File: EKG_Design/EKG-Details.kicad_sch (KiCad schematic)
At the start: 10 parts

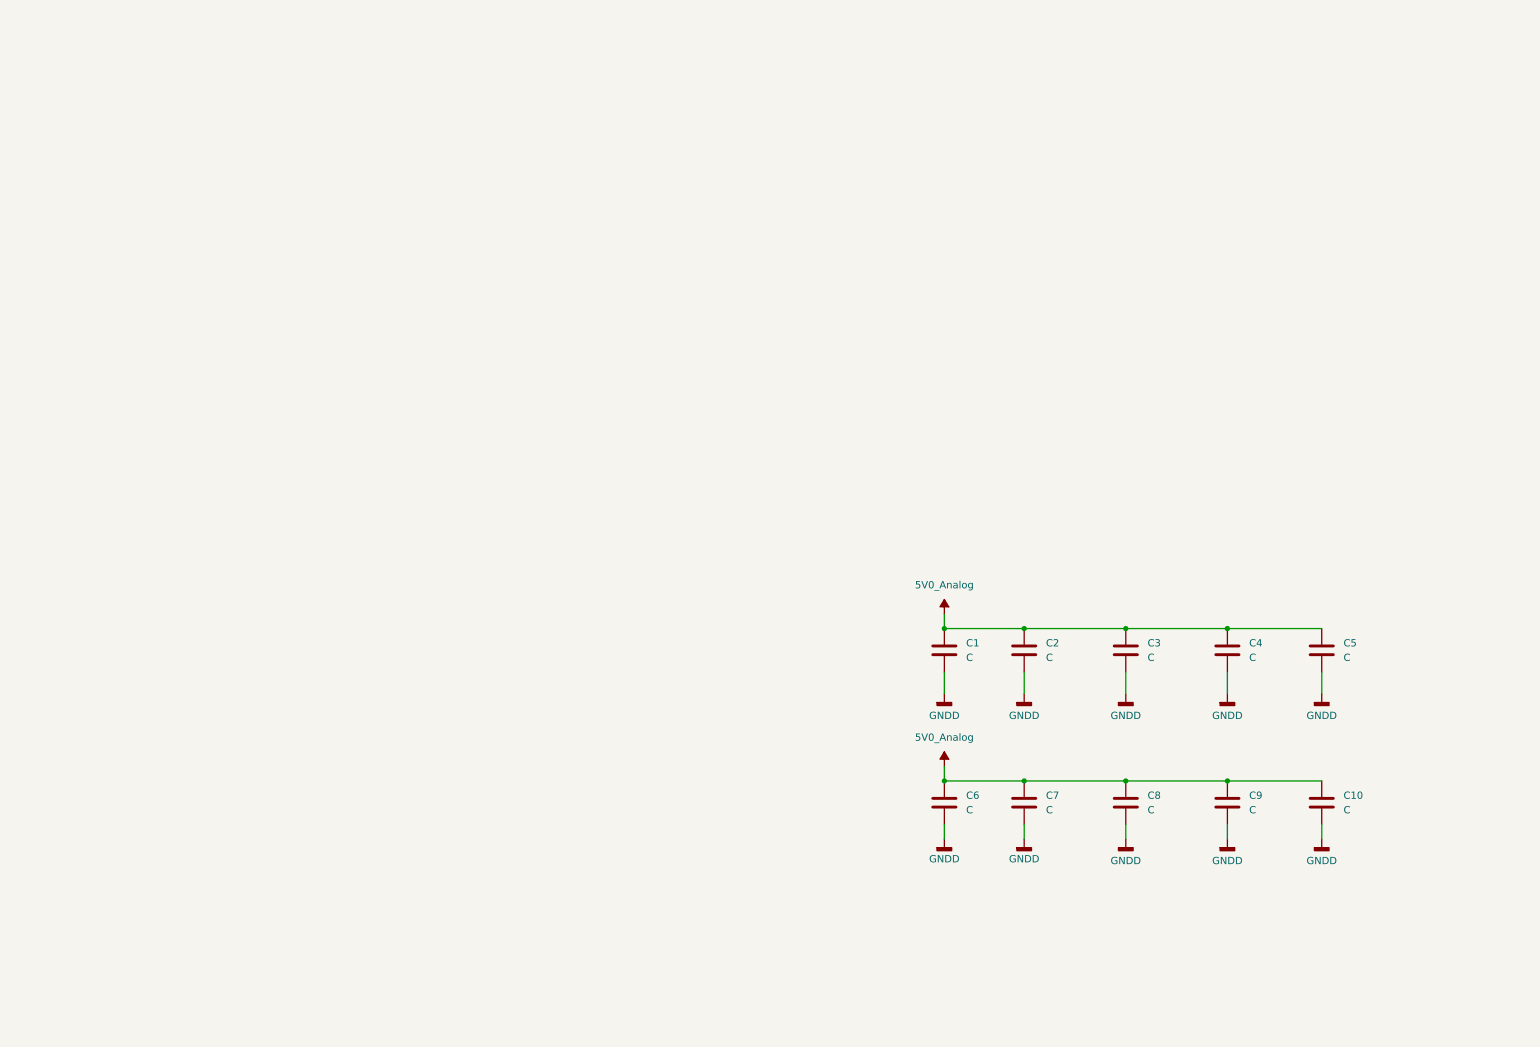
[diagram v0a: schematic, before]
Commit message: Started EKG-Details and ECG-PulseDetection Circuit Symbols implemented
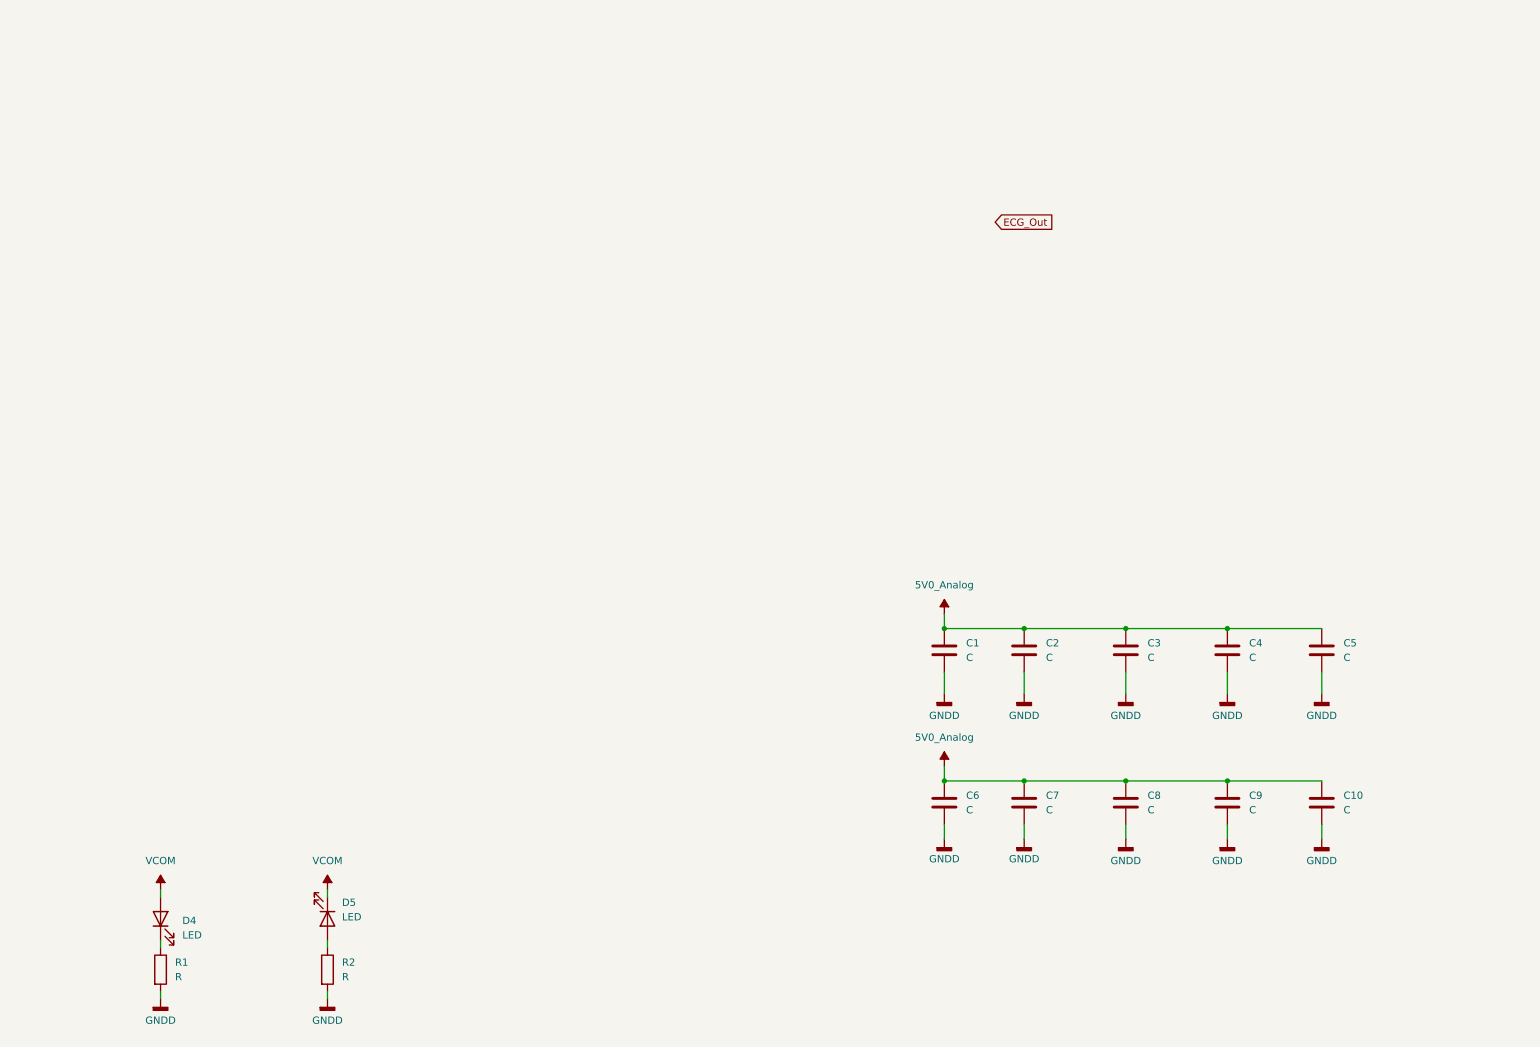
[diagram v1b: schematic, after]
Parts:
- added D4, D5: LED, symbol Device:LED
- added R1, R2: R, symbol Device:R
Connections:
- net GNDD: now also R1.2, R2.2
- new net: D4.1 (K), R1.1
- new net: D5.2 (A), R2.1
- new net VCOM: D4.2 (A), D5.1 (K)
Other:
- company: (none) -> HAWK
- title: (none) -> EKG-Verstärker

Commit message: EKG-Details updated
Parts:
- added J1, J2: Conn_01x02_Pin, symbol Connector:Conn_01x02_Pin
- added R5, R6, R7, R8: R, symbol Device:R
- added U1: OPA2156xDGK, Package_SO:VSSOP-8_3x3mm_P0.65mm, symbol Amplifier_Operational:OPA2156xDGK
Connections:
- new net: R6.2, U1.5 (+)
- new net: J2.1 (Pin_1), U1.6 (-), U1.7
- new net: J1.1 (Pin_1), R5.1
- new net: R5.2, U1.2 (-)
- new net: J1.2 (Pin_2), U1.1, U1.3 (+)
- new net: J2.2 (Pin_2), R6.1

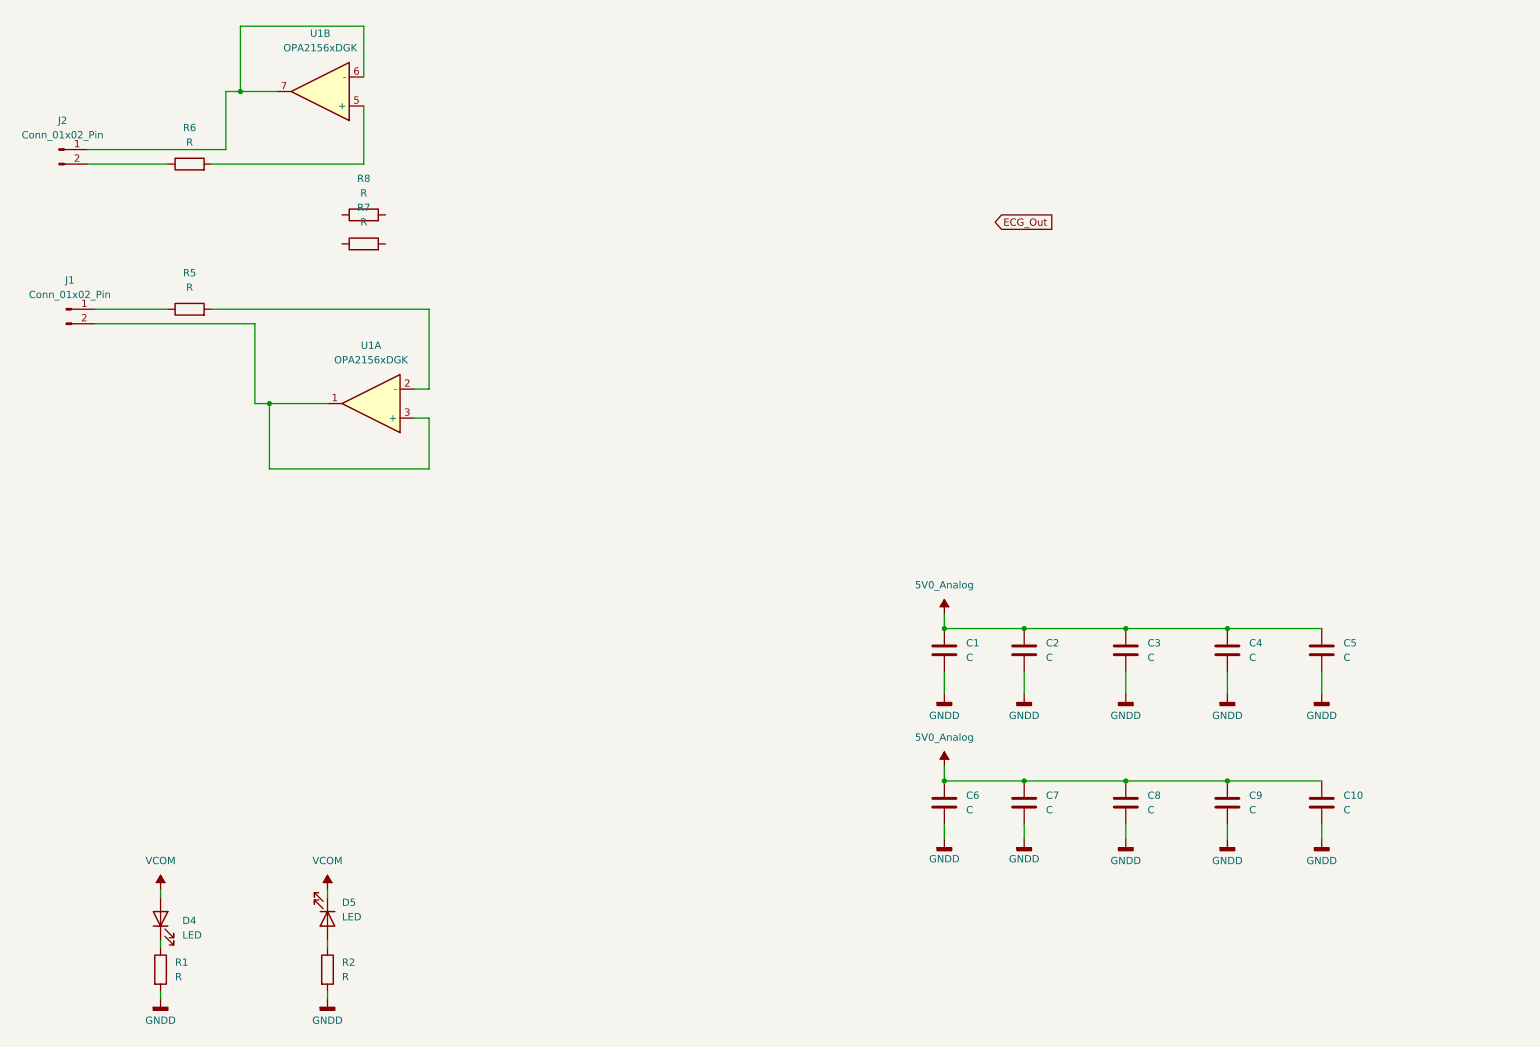
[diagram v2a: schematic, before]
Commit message: EKG-Details basic schematic, still needs cleaning
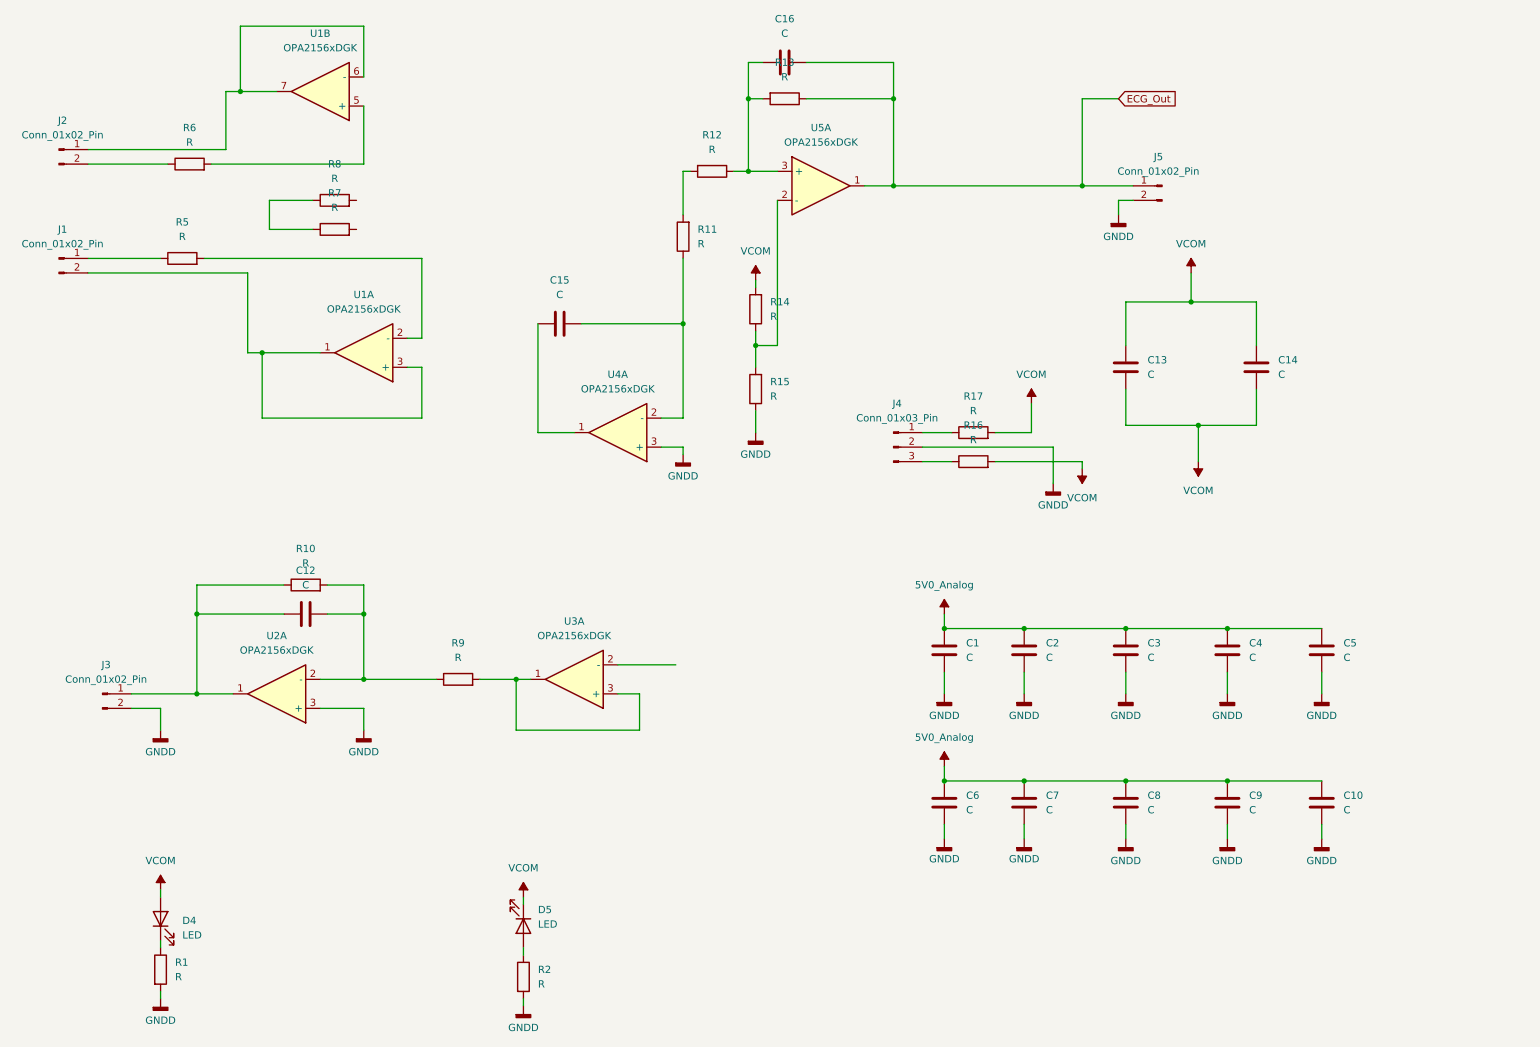
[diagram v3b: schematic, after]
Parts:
- added C12, C13, C14, C15, C16: C, symbol Device:C
- added J3, J5: Conn_01x02_Pin, symbol Connector:Conn_01x02_Pin
- added J4: Conn_01x03_Pin, symbol Connector:Conn_01x03_Pin
- added R10, R11, R12, R13, R14, R15, R16, R17, R9: R, symbol Device:R
- added U2, U3, U4, U5: OPA2156xDGK, Package_SO:VSSOP-8_3x3mm_P0.65mm, symbol Amplifier_Operational:OPA2156xDGK
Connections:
- net ECG_Out: now also C16.2, J5.1 (Pin_1), R13.1, U5.1
- net GNDD: now also J3.2 (Pin_2), J4.2 (Pin_2), J5.2 (Pin_2), R15.1, U2.3 (+), U4.3 (+)
- net VCOM: now also C13.1, C13.2, C14.1, C14.2, R14.2, R16.2, R17.2
- net at R8.1: now also R7.1
- new net: C16.1, R12.1, R13.2, U5.3 (+)
- new net: R11.2, R12.2
- new net: C12.1, J3.1 (Pin_1), R10.1, U2.1
- new net: C12.2, R10.2, R9.1, U2.2 (-)
- new net: C15.1, U4.1
- new net: C15.2, R11.1, U4.2 (-)
- new net: R14.1, R15.2, U5.2 (-)
- new net: J4.1 (Pin_1), R17.1
- new net: R9.2, U3.1, U3.3 (+)
- new net: J4.3 (Pin_3), R16.1
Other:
- moved on the sheet: D5, J1, R2, R5, R7, R8, U1A

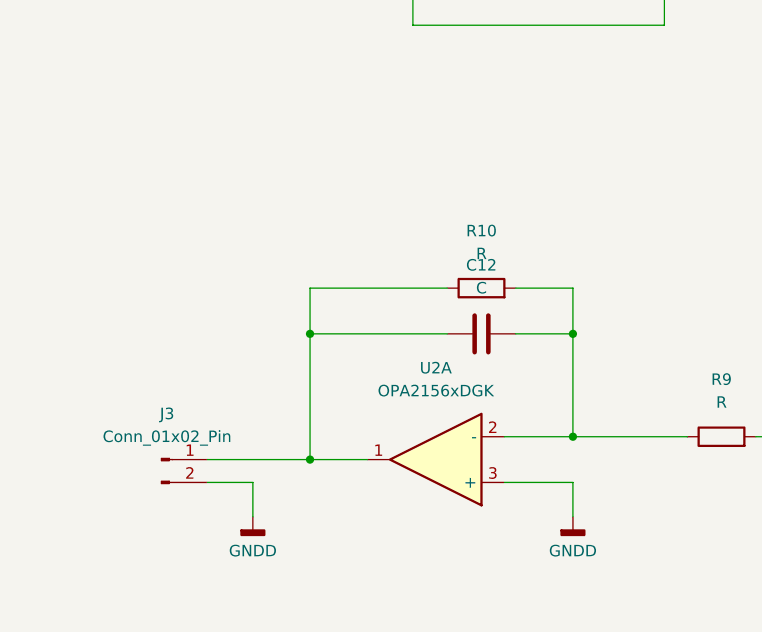
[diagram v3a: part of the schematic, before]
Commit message: EKG-Details basic schematic, still needs a little cleaning
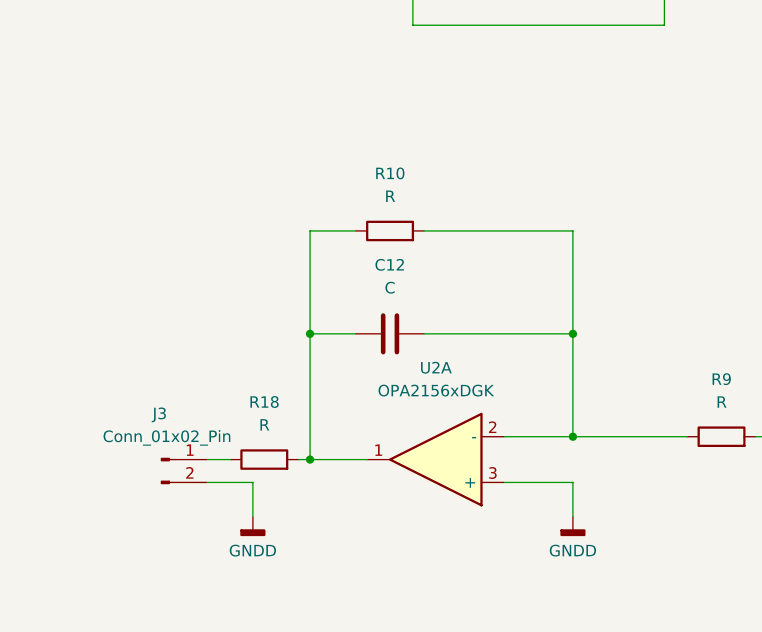
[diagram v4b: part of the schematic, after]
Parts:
- added R18: R, symbol Device:R
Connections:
- net at C12.1, R10.1, U2.1: now also R18.2; no longer J3.1 (Pin_1)
- new net: J3.1 (Pin_1), R18.1
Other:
- moved on the sheet: C12, R10
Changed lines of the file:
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@@
 	)
 	(junction
-		(at 137.16 67.31)
+		(at 52.07 118.11)
 		(diameter 0)
 		(color 0 0 0 0)
 	)
 	(junction
-		(at 227.33 85.09)
+		(at 137.16 67.31)
 		(diameter 0)
 		(color 0 0 0 0)
 	)
 	(junction
-		(at 52.07 118.11)
+		(at 227.33 85.09)
 		(diameter 0)
 		(color 0 0 0 0)
@@
 	)
 	(junction
-		(at 52.07 132.08)
+		(at 81.28 118.11)
 		(diameter 0)
 		(color 0 0 0 0)
@@
 	)
 	(junction
-		(at 81.28 118.11)
-		(diameter 0)
-		(color 0 0 0 0)
-	)
-	(junction
 		(at 107.95 129.54)
 		(diameter 0)
@@
 	)
 	(junction
+		(at 52.07 132.08)
+		(diameter 0)
+		(color 0 0 0 0)
+	)
+	(junction
 		(at 232.41 147.32)
 		(diameter 0)
@@
 	(wire
 		(pts
-			(xy 67.31 118.11) (xy 52.07 118.11)
+			(xy 57.15 118.11) (xy 52.07 118.11)
 		)
 		(stroke
@@
 	(wire
 		(pts
-			(xy 81.28 118.11) (xy 74.93 118.11)
+			(xy 81.28 118.11) (xy 64.77 118.11)
 		)
 		(stroke
@@
 	(wire
 		(pts
-			(xy 52.07 118.11) (xy 52.07 132.08)
-		)
-		(stroke
-			(width 0)
-			(type default)
-		)
-	)
-	(wire
-		(pts
 			(xy 213.36 45.72) (xy 215.9 45.72)
 		)
@@
 	(wire
 		(pts
-			(xy 81.28 113.03) (xy 81.28 118.11)
+			(xy 81.28 106.68) (xy 81.28 118.11)
 		)
 		(stroke
@@
 	(wire
 		(pts
-			(xy 40.64 132.08) (xy 52.07 132.08)
-		)
-		(stroke
-			(width 0)
-			(type default)
-		)
-	)
-	(wire
-		(pts
 			(xy 81.28 134.62) (xy 81.28 138.43)
 		)
@@
 	(wire
 		(pts
-			(xy 74.93 113.03) (xy 81.28 113.03)
+			(xy 64.77 106.68) (xy 81.28 106.68)
 		)
 		(stroke
@@
 	(wire
 		(pts
+			(xy 40.64 132.08) (xy 43.18 132.08)
+		)
+		(stroke
+			(width 0)
+			(type default)
+		)
+	)
+	(wire
+		(pts
 			(xy 111.76 86.36) (xy 118.11 86.36)
 		)
@@
 	(wire
 		(pts
+			(xy 52.07 118.11) (xy 52.07 132.08)
+		)
+		(stroke
+			(width 0)
+			(type default)
+		)
+	)
+	(wire
+		(pts
 			(xy 227.33 85.09) (xy 227.33 91.44)
 		)
@@
 	(wire
 		(pts
+			(xy 50.8 132.08) (xy 52.07 132.08)
+		)
+		(stroke
+			(width 0)
+			(type default)
+		)
+	)
+	(wire
+		(pts
 			(xy 248.92 154.94) (xy 248.92 157.48)
 		)
@@
 	(wire
 		(pts
-			(xy 52.07 113.03) (xy 67.31 113.03)
+			(xy 52.07 106.68) (xy 57.15 106.68)
 		)
 		(stroke
@@
 	(wire
 		(pts
-			(xy 52.07 118.11) (xy 52.07 113.03)
+			(xy 52.07 118.11) (xy 52.07 106.68)
 		)
 		(stroke
@@
 					(size 1.27 1.27)
 				)
+				(justify right)
 			)
 		)
@@
 	)
 	(symbol
+		(lib_id "Device:R")
+		(at 46.99 132.08 90)
+		(unit 1)
+		(body_style 1)
+		(exclude_from_sim no)
+		(in_bom yes)
+		(on_board yes)
+		(in_pos_files yes)
+		(dnp no)
+		(fields_autoplaced yes)
+		(property "Reference" "R18"
+			(at 46.99 125.73 90)
+			(show_name no)
+			(do_not_autoplace no)
+			(effects
+				(font
+					(size 1.27 1.27)
+				)
+			)
+		)
+		(property "Value" "R"
+			(at 46.99 128.27 90)
+			(show_name no)
+			(do_not_autoplace no)
+			(effects
+				(font
+					(size 1.27 1.27)
+				)
+			)
+		)
+		(property "Footprint" ""
+			(at 46.99 133.858 90)
+			(hide yes)
+			(show_name no)
+			(do_not_autoplace no)
+			(effects
+				(font
+					(size 1.27 1.27)
+				)
+			)
+		)
+		(property "Datasheet" ""
+			(at 46.99 132.08 0)
+			(hide yes)
+			(show_name no)
+			(do_not_autoplace no)
+			(effects
+				(font
+					(size 1.27 1.27)
+				)
+			)
+		)
+		(property "Description" "Resistor"
+			(at 46.99 132.08 0)
+			(hide yes)
+			(show_name no)
+			(do_not_autoplace no)
+			(effects
+				(font
+					(size 1.27 1.27)
+				)
+			)
+		)
+		(pin "2"
+		)
+		(pin "1"
+		)
+		(instances
+			(project "EKG_Design"
+				(path "/145a8612-0e2a-4b7d-8919-051e741c5f83/fe31fbed-a3d6-4e29-8087-8265cc4e44fa"
+					(reference "R18")
+					(unit 1)
+				)
+			)
+		)
+	)
+	(symbol
 		(lib_id "power:VCOM")
 		(at 149.86 59.69 0)
@@
 	(symbol
 		(lib_id "Device:C")
-		(at 71.12 118.11 90)
+		(at 60.96 118.11 90)
 		(unit 1)
 		(body_style 1)
@@
 		(fields_autoplaced yes)
 		(property "Reference" "C12"
-			(at 71.12 110.49 90)
+			(at 60.96 110.49 90)
 			(show_name no)
 			(do_not_autoplace no)
@@
 		)
 		(property "Value" "C"
-			(at 71.12 113.03 90)
+			(at 60.96 113.03 90)
 			(show_name no)
 			(do_not_autoplace no)
@@
 		)
 		(property "Footprint" ""
-			(at 74.93 117.1448 0)
+			(at 64.77 117.1448 0)
 			(hide yes)
 			(show_name no)
@@
 		)
 		(property "Datasheet" ""
-			(at 71.12 118.11 0)
+			(at 60.96 118.11 0)
 			(hide yes)
 			(show_name no)
@@
 		)
 		(property "Description" "Unpolarized capacitor"
-			(at 71.12 118.11 0)
+			(at 60.96 118.11 0)
 			(hide yes)
 			(show_name no)
@@
 	(symbol
 		(lib_id "Device:R")
-		(at 71.12 113.03 90)
+		(at 60.96 106.68 90)
 		(unit 1)
 		(body_style 1)
@@
 		(fields_autoplaced yes)
 		(property "Reference" "R10"
-			(at 71.12 106.68 90)
+			(at 60.96 100.33 90)
 			(show_name no)
 			(do_not_autoplace no)
@@
 		)
 		(property "Value" "R"
-			(at 71.12 109.22 90)
+			(at 60.96 102.87 90)
 			(show_name no)
 			(do_not_autoplace no)
@@
 		)
 		(property "Footprint" ""
-			(at 71.12 114.808 90)
+			(at 60.96 108.458 90)
 			(hide yes)
 			(show_name no)
@@
 		)
 		(property "Datasheet" ""
-			(at 71.12 113.03 0)
+			(at 60.96 106.68 0)
 			(hide yes)
 			(show_name no)
@@
 		)
 		(property "Description" "Resistor"
-			(at 71.12 113.03 0)
+			(at 60.96 106.68 0)
 			(hide yes)
 			(show_name no)
